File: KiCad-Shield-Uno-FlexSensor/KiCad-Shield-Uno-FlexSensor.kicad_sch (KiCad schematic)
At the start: 10 parts, among them J1 Power, J2 Digital/PWM, J3 Analog, J4 Digital/PWM

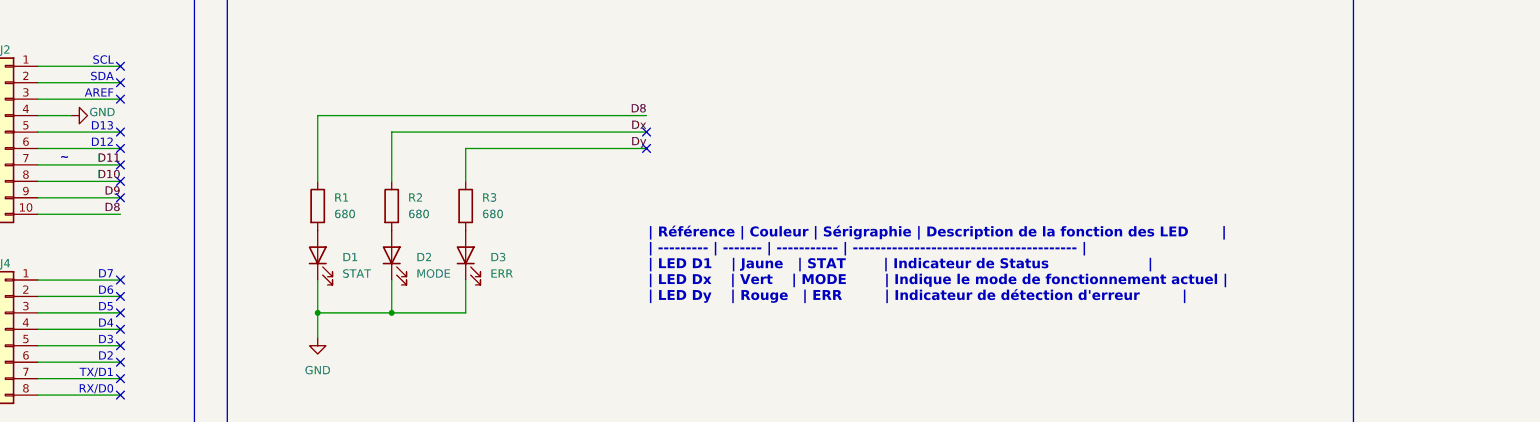
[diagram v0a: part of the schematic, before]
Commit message: Ajout des contraintes du design manager pour le routage à l'INSA
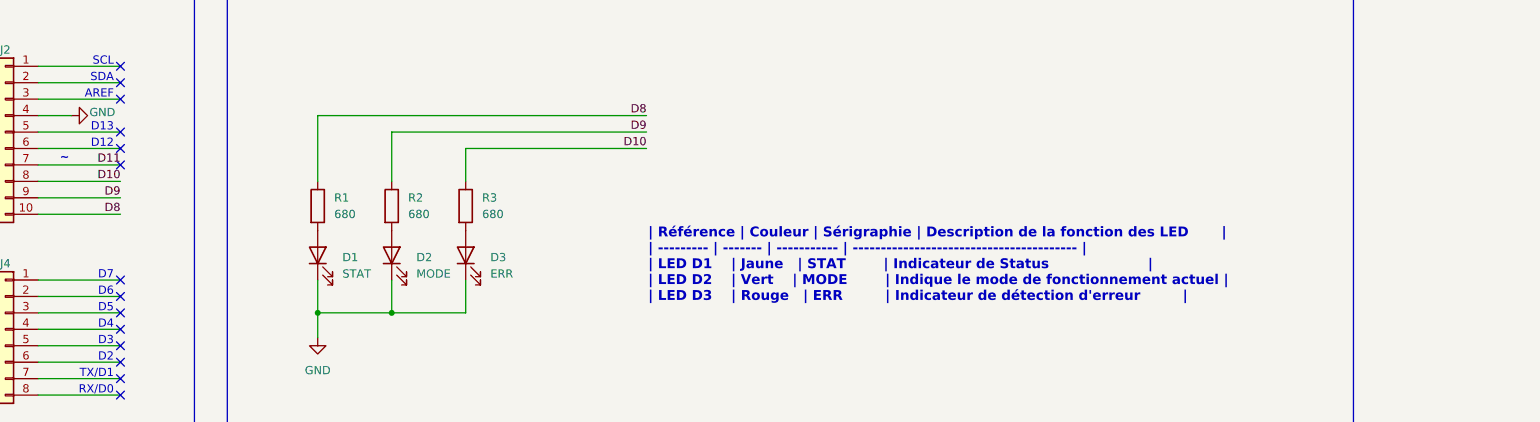
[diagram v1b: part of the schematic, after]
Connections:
- net Dx is gone; now on net D9: R2.1
- net Dy is gone; now on net D10: R3.1
- no-connect marks 27 -> 23
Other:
- note added: "| Référence | Couleur | Sérigraphie | Description de la fonction des LED | | --------- | ------- | ----------- | ---------------------------------------- | | LED D1 | Jaune | STAT | Indicateur de Status | | LED D2 | Vert | MODE | Indique le mode de fonctionnement actuel | | LED D3 | Rouge | ERR | Indicateur de détection d'erreur |"
- note removed: "| Référence | Couleur | Sérigraphie | Description de la fonction des LED | | --------- | ------- | ----------- | ---------------------------------------- | | LED D1 | Jaune | STAT | Indicateur de Status | | LED Dx | Vert | MODE | Indique le mode de fonctionnement actuel | | LED Dy | Rouge | ERR | Indicateur de détection d'erreur |"
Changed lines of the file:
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@@
 		)
 	)
-	(text "| Référence | Couleur | Sérigraphie | Description de la fonction des LED       |\n| --------- | ------- | ----------- | ---------------------------------------- |\n| LED D1    | Jaune   | STAT        | Indicateur de Status                     |\n| LED Dx    | Vert    | MODE        | Indique le mode de fonctionnement actuel |\n| LED Dy    | Rouge   | ERR         | Indicateur de détection d'erreur         |"
+	(text "| Référence | Couleur | Sérigraphie | Description de la fonction des LED       |\n| --------- | ------- | ----------- | ---------------------------------------- |\n| LED D1    | Jaune   | STAT        | Indicateur de Status                     |\n| LED D2    | Vert    | MODE        | Indique le mode de fonctionnement actuel |\n| LED D3    | Rouge   | ERR         | Indicateur de détection d'erreur         |"
 		(exclude_from_sim no)
 		(at 171.704 70.104 0)
@@
 	)
 	(no_connect
-		(at 90.17 59.69)
-	)
-	(no_connect
 		(at 90.17 39.37)
 	)
 	(no_connect
-		(at 171.45 52.07)
-	)
-	(no_connect
 		(at 90.17 72.39)
 	)
@@
 	)
 	(no_connect
-		(at 171.45 49.53)
-	)
-	(no_connect
 		(at 36.83 85.09)
 	)
 	(no_connect
 		(at 36.83 82.55)
-	)
-	(no_connect
-		(at 90.17 57.15)
 	)
 	(no_connect
@@
 		)
 	)
-	(label "Dy"
+	(label "D10"
 		(at 171.45 52.07 180)
 		(effects
@@
 		)
 	)
-	(label "Dx"
+	(label "D9"
 		(at 171.45 49.53 180)
 		(effects
